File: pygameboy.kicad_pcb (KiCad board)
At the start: 2 copper layers, 56 x 60.7 mm, 133 parts, among them J1 Conn_01x01, J14 Conn_01x04, J2 Conn_01x01, J4 USB_C_Receptacle_USB2.0_16P, J5 AudioJack4, J6 AudioJack4, Q1 BSS138, SW1 SW_Push, SW2 SW_Push, U1 CARTRIDGE, U201 W25Q128JVS, U202 RP2350_80QFN, U5 74x4245, U7 AP2204K-3.3, U8 H11L1, Y201 ABM8-272-T3

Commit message: Update to v8
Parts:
- added G***: LOGO, chickadee:chickadee_2mm_fcu, F.Cu at (125.2, 77.5)
- added J101: Conn_01x03, Connector_JST:JST_SH_BM03B-SRSS-TB_1x03-1MP_P1.00mm_Vertical, F.Cu at (145.6, 53.5)
- moved R3 7.56 mm to (131.2, 71.6)
- moved FID0 5.60 mm to (138.2, 53.0)
- moved C212 2.62 mm to (141.5, 67.8), turned to 90 degrees
- moved C16 1.62 mm to (144.8, 50.2)
- moved R1 1.62 mm to (142.8, 50.2)
- moved R204 1.31 mm to (146.8, 50.3), turned to 0 degrees
- moved C102 0.98 mm to (146.5, 56.9), turned to 180 degrees
- moved C217 0.92 mm to (134.0, 72.2), turned to -135 degrees
- moved C210 0.86 mm to (142.4, 59.7), turned to 90 degrees
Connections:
- U202 pad 22: /RP2350 Core/GPIO22 -> /DATA_OE
- U202 pad 23: /RP2350 Core/GPIO23 -> /3V_D0
- U202 pad 25: /RP2350 Core/GPIO24 -> /3V_D1
- U202 pad 26: /RP2350 Core/GPIO25 -> /3V_D2
- U202 pad 27: /RP2350 Core/GPIO26 -> /3V_D3
- U202 pad 28: /RP2350 Core/GPIO27 -> /3V_D4
- U202 pad 36: /DATA_OE -> /3V_D5
- U202 pad 37: /3V_D0 -> /3V_D6
- U202 pad 38: /3V_D1 -> /3V_D7
- U202 pad 39: /3V_D2 -> /RP_GB_RESET
- U202 pad 40: /3V_D3 -> /RP2350 Core/GPIO32
- U202 pad 42: /3V_D4 -> /RP2350 Core/GPIO33
- U202 pad 43: /3V_D5 -> /RP2350 Core/GPIO34
- U202 pad 44: /3V_D6 -> /RP2350 Core/GPIO35
- U202 pad 45: /3V_D7 -> /RP2350 Core/GPIO36
- U202 pad 46: /RP_GB_RESET -> /RP2350 Core/GPIO37
- U202 pad 53: /RP2350 Core/GPIO42_ADC2 -> /DEBUG_TX
- U202 pad 54: /RP2350 Core/GPIO43_ADC3 -> /DEBUG_RX
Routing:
- net /DEBUG_TX: track 0.00 -> 12.9 mm
- net /DEBUG_RX: track 0.00 -> 11.6 mm
- net /DATA_OE: track 7.26 -> 15.3 mm, vias 0 -> 2
- net /3V_D0: track 7.42 -> 14.8 mm, vias 0 -> 2
- net /3V_D2: track 7.65 -> 14.6 mm, vias 0 -> 2
- net /3V_D4: track 8.82 -> 15.2 mm, vias 0 -> 2
- net GND: track 41.6 -> 47.3 mm, vias 43 -> 45
- net /3V_D3: track 7.67 -> 13.3 mm, vias 0 -> 2
- net /3V_D1: track 7.53 -> 12.9 mm, vias 0 -> 2
- net /RP_GB_RESET: track 8.37 -> 11.1 mm
- net +3V3: track 151.1 -> 153.7 mm
- net /LED: track 30.2 -> 28.4 mm
- net /SDA: track 24.8 -> 23.2 mm
- net /SCL: track 24.5 -> 22.9 mm
- net /RP2350 Core/QSPI_SS: track 41.3 -> 39.7 mm
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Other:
- board text added: "AUDIO FILTER"
- board text added: "MIDI"
- board text added: "StemmaQT"
- board text added: "UART"

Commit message: WIP v9
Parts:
- added C103: 10uF, Capacitor_SMD:C_0805_2012Metric, F.Cu at (94.0, 66.0)
- added C104: 10uF, Capacitor_SMD:C_0805_2012Metric, F.Cu at (94.1, 68.8)
- added C105: 10uF, Capacitor_SMD:C_0805_2012Metric, F.Cu at (94.0, 72.0)
- added C106: 10uF, Capacitor_SMD:C_0805_2012Metric, F.Cu at (94.0, 75.0)
- added C107: 100n, Capacitor_SMD:C_0402_1005Metric, F.Cu at (138.4, 54.0)
- added D101: WS2812B-2020, LED_SMD:LED_WS2812B-2020_PLCC4_2.0x2.0mm, F.Cu at (138.3, 52.2)
- added D201: 1N4148W, Diode_SMD:D_SOD-123, F.Cu at (155.5, 48.2)
- added J102: Conn_01x03, Connector_JST:JST_SH_BM03B-SRSS-TB_1x03-1MP_P1.00mm_Vertical, F.Cu at (155.7, 60.5)
- added RN101: 4x1k, Resistor_SMD:R_Array_Convex_4x0603, F.Cu at (104.3, 85.3)
- added RN102: 4x1k, Resistor_SMD:R_Array_Convex_4x0603, F.Cu at (110.8, 84.8)
- added RN103: 4x1k, Resistor_SMD:R_Array_Convex_4x0603, F.Cu at (117.0, 84.9)
- added RN104: 4x1k, Resistor_SMD:R_Array_Convex_4x0603, F.Cu at (118.5, 80.5)
- added RN105: 4x1k, Resistor_SMD:R_Array_Convex_4x0603, F.Cu at (130.5, 83.8)
- added RN106: 4x1k, Resistor_SMD:R_Array_Convex_4x0603, F.Cu at (135.4, 87.6)
- added RN107: 4x1k, Resistor_SMD:R_Array_Convex_4x0603, F.Cu at (141.3, 87.5)
- C10, C13: footprint Capacitor_SMD:C_0402_1005Metric -> Capacitor_SMD:C_0603_1608Metric
- C207, C208: footprint Capacitor_SMD:C_0402_1005Metric -> Capacitor_SMD:C_0805_2012Metric
- D1, D2: value MBR120 -> MBR0540
- U7: value AP2204K-3.3 -> AP2212-3.3
- moved FID1 25.4 mm to (104.1, 79.4)
- moved FID0 12.7 mm to (138.2, 40.3)
- moved D1 6.12 mm to (122.7, 48.8), turned to 90 degrees
- moved D4 5.53 mm to (106.4, 53.7), turned to 180 degrees
- moved R5 0.85 mm to (109.4, 52.8)
- moved U201 0.14 mm to (128.5, 52.0)
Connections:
- net +BATT renamed VCC
- D3 pad 2: +3V3 -> /LED
- R204 pad 2: /BOOT -> Net-(D201-A)
- R4 pad 2: /LED -> GND
- U1 pad 10: /A4 -> Net-(RN103-R4.2)
- U1 pad 11: /A5 -> Net-(RN103-R3.2)
- U1 pad 12: /A6 -> Net-(RN103-R2.2)
- U1 pad 13: /A7 -> Net-(RN103-R1.2)
- U1 pad 14: /A8 -> Net-(RN104-R4.2)
- U1 pad 15: /A9 -> Net-(RN104-R3.2)
- U1 pad 16: /A10 -> Net-(RN104-R2.2)
- U1 pad 17: /A11 -> Net-(RN104-R1.2)
- U1 pad 18: /A12 -> Net-(RN105-R4.2)
- U1 pad 19: /A13 -> Net-(RN105-R3.2)
- U1 pad 2: /CLK -> Net-(RN101-R4.2)
- U1 pad 20: /A14 -> Net-(RN105-R2.2)
- U1 pad 21: /A15 -> Net-(RN105-R1.2)
- U1 pad 22: /D0 -> Net-(RN106-R4.2)
- U1 pad 23: /D1 -> Net-(RN106-R3.2)
- U1 pad 24: /D2 -> Net-(RN106-R2.2)
- U1 pad 25: /D3 -> Net-(RN106-R1.2)
- U1 pad 26: /D4 -> Net-(RN107-R4.2)
- U1 pad 27: /D5 -> Net-(RN107-R3.2)
- U1 pad 28: /D6 -> Net-(RN107-R2.2)
- U1 pad 29: /D7 -> Net-(RN107-R1.2)
- U1 pad 3: /WR -> Net-(RN101-R3.2)
- U1 pad 4: /RD -> Net-(RN101-R2.2)
- U1 pad 5: /CS -> Net-(RN101-R1.2)
- U1 pad 6: /A0 -> Net-(RN102-R4.2)
- U1 pad 7: /A1 -> Net-(RN102-R3.2)
- U1 pad 8: /A2 -> Net-(RN102-R2.2)
- U1 pad 9: /A3 -> Net-(RN102-R1.2)
- U202 pad 1: /A2 -> /RD
- U202 pad 11: /A10 -> /A6
- U202 pad 12: /A11 -> /A7
- U202 pad 13: /A12 -> /A8
- U202 pad 14: /A13 -> /A9
- U202 pad 16: /A14 -> /A10
- U202 pad 17: /A15 -> /A11
- U202 pad 18: /CLK -> /A12
- U202 pad 19: /WR -> /A13
- U202 pad 2: /A3 -> /CS
- U202 pad 20: /RD -> /A14
- U202 pad 21: /CS -> /A15
- U202 pad 3: /A4 -> /A0
- U202 pad 33: /RP2350 Core/SWCLK -> /SWCLK
- U202 pad 34: /RP2350 Core/SWD -> /SWD
- U202 pad 4: /A5 -> /A1
- U202 pad 52: /RP2350 Core/GPIO41_ADC1 -> /BOOT
- U202 pad 55: /RP2350 Core/GPIO44_ADC4 -> /NEOPIXEL
- U202 pad 6: /A6 -> /A2
- U202 pad 7: /A7 -> /A3
- U202 pad 79: /A0 -> /CLK
- U202 pad 8: /A8 -> /A4
- U202 pad 80: /A1 -> /WR
- U202 pad 9: /A9 -> /A5
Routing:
- net /CLK: track 58.9 -> 11.5 mm, vias 3 -> 1
- net /A0: track 57.4 -> 11.5 mm, vias 3 -> 1
- net /WR: track 60.0 -> 14.5 mm, vias 3 -> 1
- net /RD: track 94.3 -> 50.6 mm, vias 4 -> 2
- net /CS: track 58.0 -> 14.5 mm, vias 3 -> 1
- net /A1: track 57.5 -> 15.2 mm
- net /A2: track 52.6 -> 11.5 mm
- net /A3: track 54.5 -> 14.5 mm
- net /A4: track 50.3 -> 11.5 mm
- net /A5: track 52.2 -> 14.5 mm
- net /A6: track 47.9 -> 11.5 mm
- net /A7: track 50.7 -> 14.5 mm
- net /A8: track 47.6 -> 11.5 mm
- net /A10: track 43.1 -> 11.5 mm, vias 1 -> 0
- net /A11: track 45.4 -> 14.5 mm
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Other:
- board text added: "10, 4.7 should be 0805. 1uf 0603. 0.1 0402"
- board text added: "Boot button diode."
- board text added: "Can move RP2350 down."
- board text added: "Connect ground"
- board text added: "NeoPixel"
- board text added: "PSRAM Here"
- board text added: "Scorpio has smaller level shifter"
- board text added: "Shift lower left cap down"
- board text added: "Smaller fiducials."
- board text added: "Squeeze diodes."
- board text added: "Tie stemma mounting points to ground"

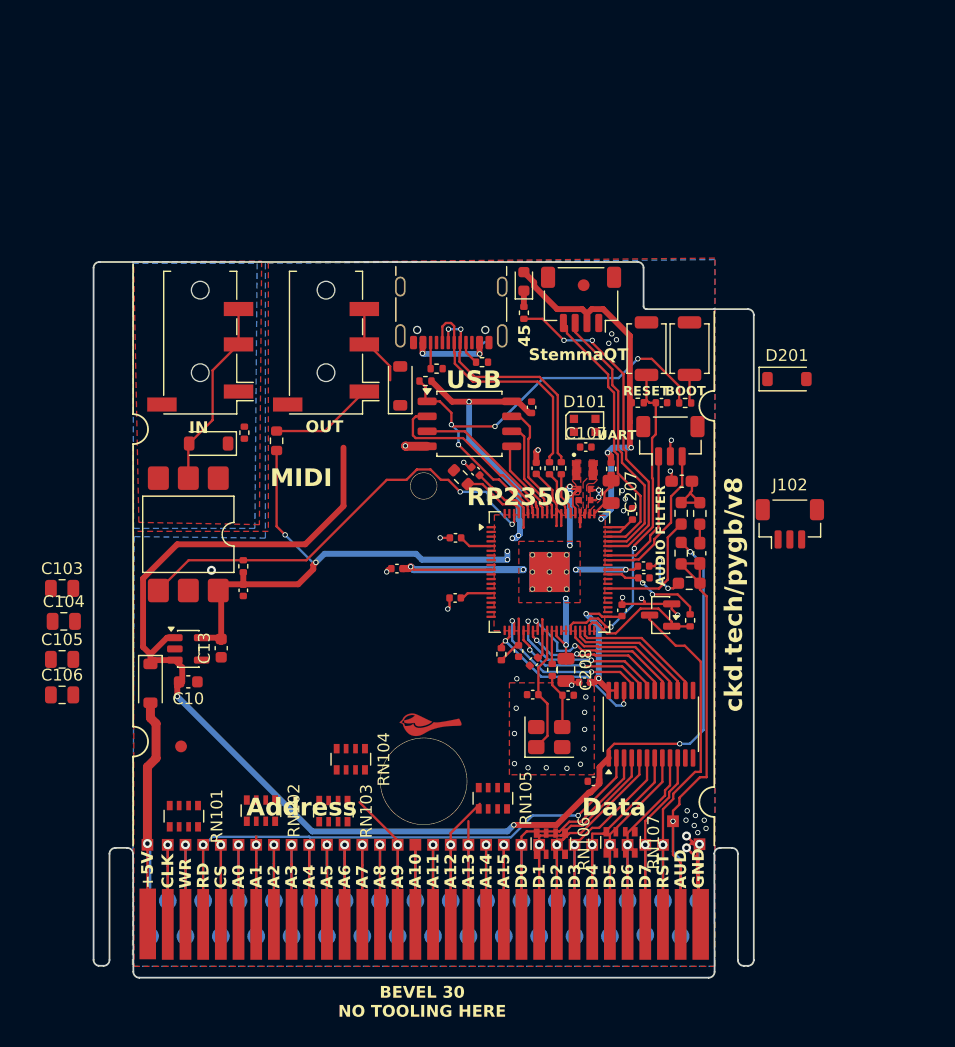
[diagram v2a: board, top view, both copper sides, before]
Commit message: Half routed. microsd added
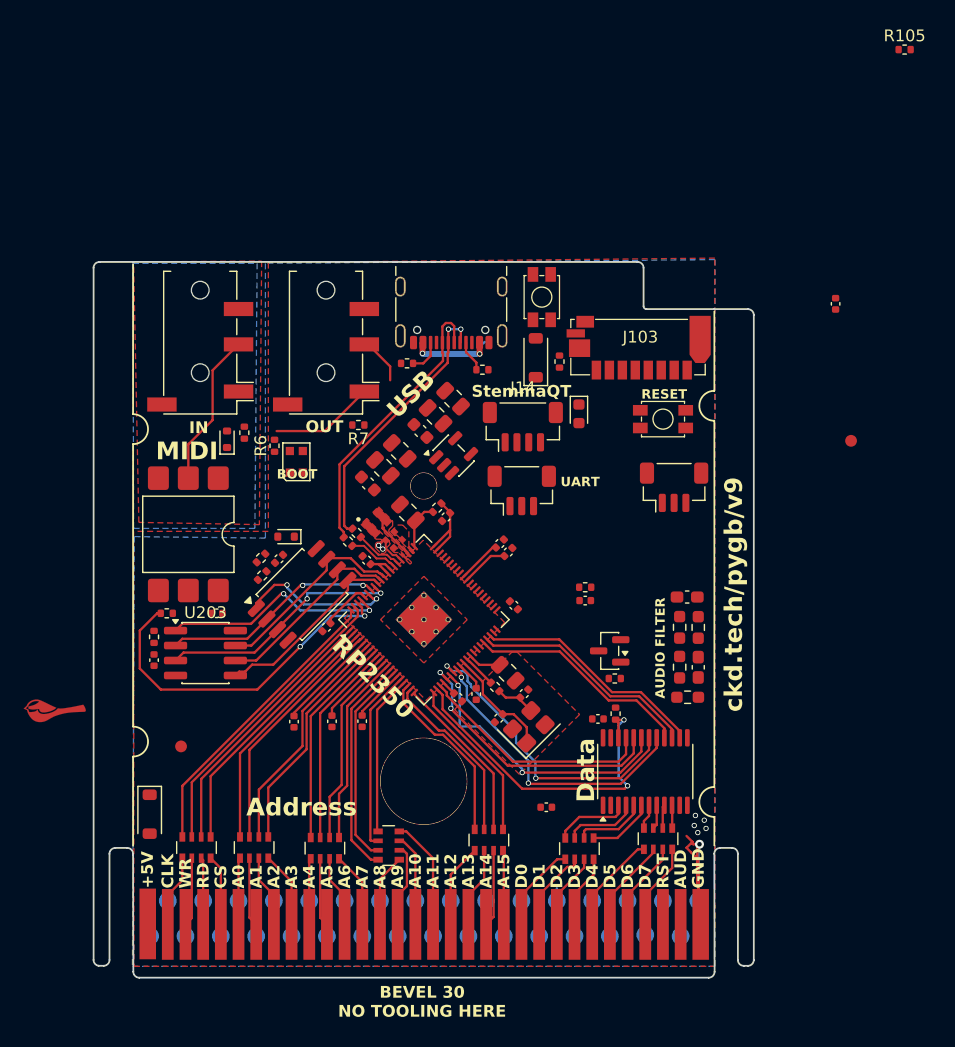
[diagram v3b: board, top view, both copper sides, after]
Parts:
- removed TP1, TP10, TP11, TP12, TP13, TP14, TP15, TP16, TP17, TP18, TP19, TP2, TP20, TP21, TP22, TP23, TP24, TP25, TP26, TP27, TP28, TP29, TP3, TP30, TP31, TP32, TP4, TP5, TP6, TP7, TP8, TP9: Test_Point, gameboy:Test Point
- added C219: 100n, Capacitor_SMD:C_0402_1005Metric, F.Cu at (101.8, 72.1)
- added J103: Micro_SD_Card, Adafruit:TF-027-HXXX, F.Cu at (142.8, 45.4)
- added R105: 10k, Resistor_SMD:R_0402_1005Metric, F.Cu at (165.4, 20.3)
- added R208: 10k, Resistor_SMD:R_0402_1005Metric, F.Cu at (101.8, 70.1)
- added U203: APS6404L-3SQR-ZR, Package_SO:SOP-8_3.76x4.96mm_P1.27mm, F.Cu at (106.1, 71.5)
- D201, D4: footprint Diode_SMD:D_SOD-123 -> Diode_SMD:D_SOD-523
- J14: footprint Connector_JST:JST_SH_SM04B-SRSS-TB_1x04-1MP_P1.00mm_Horizontal -> Connector_JST:JST_SH_BM04B-SRSS-TB_1x04-1MP_P1.00mm_Vertical
- R6, R7: footprint Resistor_SMD:R_0603_1608Metric -> Resistor_SMD:R_0402_1005Metric
- SW1, SW2: footprint Button_Switch_SMD:SW_SPST_TS-1088-xR020 -> Adafruit:TS-1185
- moved D201 44.5 mm to (113.0, 61.6), turned to 180 degrees
- moved C105 39.9 mm to (127.1, 49.9), turned to -45 degrees
- moved C106 39.5 mm to (125.7, 51.4), turned to -45 degrees
- moved R204 38.3 mm to (110.8, 63.4), turned to 45 degrees
- moved C104 32.0 mm to (122.6, 54.3), turned to -45 degrees
- moved G*** 31.9 mm to (93.3, 76.4)
- moved C103 29.1 mm to (121.2, 55.8), turned to -45 degrees
- moved U7 27.8 mm to (127.2, 54.7), turned to 45 degrees
- moved C210 27.7 mm to (116.4, 69.3), turned to -135 degrees
- moved FID0 26.2 mm to (160.9, 53.5)
- moved C13 25.0 mm to (124.4, 52.6), turned to -45 degrees
- moved C201 25.0 mm to (112.4, 63.5), turned to 45 degrees
- moved D101 24.7 mm to (113.8, 55.2), turned to 90 degrees
- moved C107 24.4 mm to (159.6, 41.9), turned to 90 degrees
- moved C10 22.7 mm to (119.9, 57.1), turned to -45 degrees
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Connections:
- J5 pad R2: Net-(D4-A) -> /SHIELD
- J6 pad R2: Net-(J6-PadR1) -> GND
- U202 pad 40: /RP2350 Core/GPIO32 -> /PWM_AUDIO
- U202 pad 42: /RP2350 Core/GPIO33 -> /SD_DAT3_CS
- U202 pad 43: /RP2350 Core/GPIO34 -> /SD_CLK
- U202 pad 44: /RP2350 Core/GPIO35 -> /SD_CMD_MOSI
- U202 pad 45: /RP2350 Core/GPIO36 -> /SD_DAT0_MISO
- U202 pad 46: /RP2350 Core/GPIO37 -> /SD_DAT1
- U202 pad 47: /PWM_AUDIO -> /SD_DAT2
- U202 pad 48: /RP2350 Core/GPIO39 -> /SD_DAT3_CS
- U202 pad 77: /MIDI_OUT -> /RP2350 Core/GPIO0
- U202 pad 79: /CLK -> /WR
- U202 pad 80: /WR -> /CLK
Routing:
- net +3V3: track 153.7 -> 35.1 mm, vias 14 -> 0
- net +5V: track 111.3 -> 0.00 mm, vias 4 -> 0
- net /AUD: track 46.5 -> 0.00 mm, vias 1 -> 0
- net /GB_RESET: track 34.9 -> 0.00 mm, vias 1 -> 0
- net /LED: track 28.4 -> 0.00 mm, vias 2 -> 0
- net /RESET: track 28.4 -> 0.00 mm, vias 2 -> 0
- net /RD: track 50.6 -> 22.9 mm, vias 2 -> 0
- net VCC: track 27.4 -> 0.32 mm, vias 1 -> 0
- net /RP2350 Core/QSPI_SS: track 40.2 -> 13.3 mm, vias 4 -> 2
- net +1V1: track 40.5 -> 17.1 mm, vias 9 -> 2
- net /SDA: track 23.2 -> 0.00 mm
- net GND: track 47.5 -> 24.6 mm, vias 45 -> 6
- net /SCL: track 22.9 -> 0.00 mm
- net /D5: track 23.7 -> 2.05 mm, vias 1 -> 0
- net /D7: track 22.9 -> 1.94 mm, vias 1 -> 0
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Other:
- board text added: "Nothing to interact with below"
- board text added: "ckd.tech/pygb/v9"
- board text removed: "45"
- board text removed: "Boot button diode."
- board text removed: "Can move RP2350 down."
- board text removed: "Connect ground"
- board text removed: "NeoPixel"
- board text removed: "PSRAM Here"
- board text removed: "Scorpio has smaller level shifter"
- board text removed: "Shift lower left cap down"
- board text removed: "Smaller fiducials."
- board text removed: "Squeeze diodes."
- board text removed: "ckd.tech/pygb/v8"

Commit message: Final draft of v9
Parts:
- moved G*** 59.2 mm to (139.9, 39.9)
- moved C107 45.8 mm to (115.8, 55.3), turned to -90 degrees
- moved R105 43.4 mm to (138.8, 54.5), turned to 45 degrees
- moved FID0 13.6 mm to (151.1, 44.1)
- moved R7 5.35 mm to (122.4, 47.9)
- moved R1 5.31 mm to (133.0, 66.0), turned to 45 degrees
- moved C16 4.61 mm to (133.8, 66.7), turned to -135 degrees
- moved R6 4.30 mm to (116.3, 53.6), turned to 0 degrees
- moved C102 4.16 mm to (147.0, 62.6)
- moved R101 3.40 mm to (144.8, 66.3)
- moved R102 3.03 mm to (148.1, 66.3)
- moved R4 2.59 mm to (137.3, 49.1), turned to 180 degrees
- moved R103 2.17 mm to (144.7, 71.2)
- moved C7 1.79 mm to (133.5, 85.4), turned to 90 degrees
- moved D1 1.49 mm to (133.1, 47.5), turned to 0 degrees
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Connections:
- J101 pad MP: (no net) -> GND
- J102 pad MP: (no net) -> GND
- J14 pad MP: (no net) -> GND
- U202 pad 49: /RP2350 Core/GPIO40_ADC0 -> /NEOPIXEL
- U202 pad 55: /NEOPIXEL -> /MIDI_OUT
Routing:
- net +5V: track 0.00 -> 157.3 mm, vias 0 -> 9
- net +3V3: track 35.1 -> 172.8 mm, vias 0 -> 14
- net /NEOPIXEL: track 0.00 -> 56.4 mm, vias 0 -> 2
- net /BOOT: track 0.00 -> 55.1 mm, vias 0 -> 4
- net /RD: track 22.9 -> 70.4 mm, vias 0 -> 1
- net /AUD: track 0.00 -> 33.7 mm, vias 0 -> 1
- net /GB_RESET: track 0.00 -> 33.1 mm, vias 0 -> 1
- net /SD_DAT3_CS: track 0.00 -> 31.0 mm, vias 0 -> 2
- net /RESET: track 0.00 -> 30.7 mm
- net GND: track 24.6 -> 54.5 mm, vias 6 -> 98
- net /SD_DAT1: track 0.00 -> 27.6 mm
- net /SD_DAT0_MISO: track 0.00 -> 27.6 mm, vias 0 -> 2
- net /SD_CLK: track 0.00 -> 26.7 mm, vias 0 -> 2
- net /SWD: track 0.00 -> 25.9 mm, vias 0 -> 2
- net +1V1: track 17.1 -> 42.7 mm, vias 2 -> 9
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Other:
- board text added: "FLASH"
- board text added: "GB RESET"
- board text added: "MICROSD"
- board text added: "PSRAM"
- board text added: "SWD"
- board text removed: "Tie stemma mounting points to ground"
